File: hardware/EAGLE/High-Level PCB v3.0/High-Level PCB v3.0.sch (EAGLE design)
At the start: 28 parts, among them IC1 DS8921, IC2 DS8921, J1 Micro-SD, J2 Gyro, J3 Compass, J4 GPS, J5 CAN BUS, X1 RJ45, X2 Vehicle control, X4 RJ45

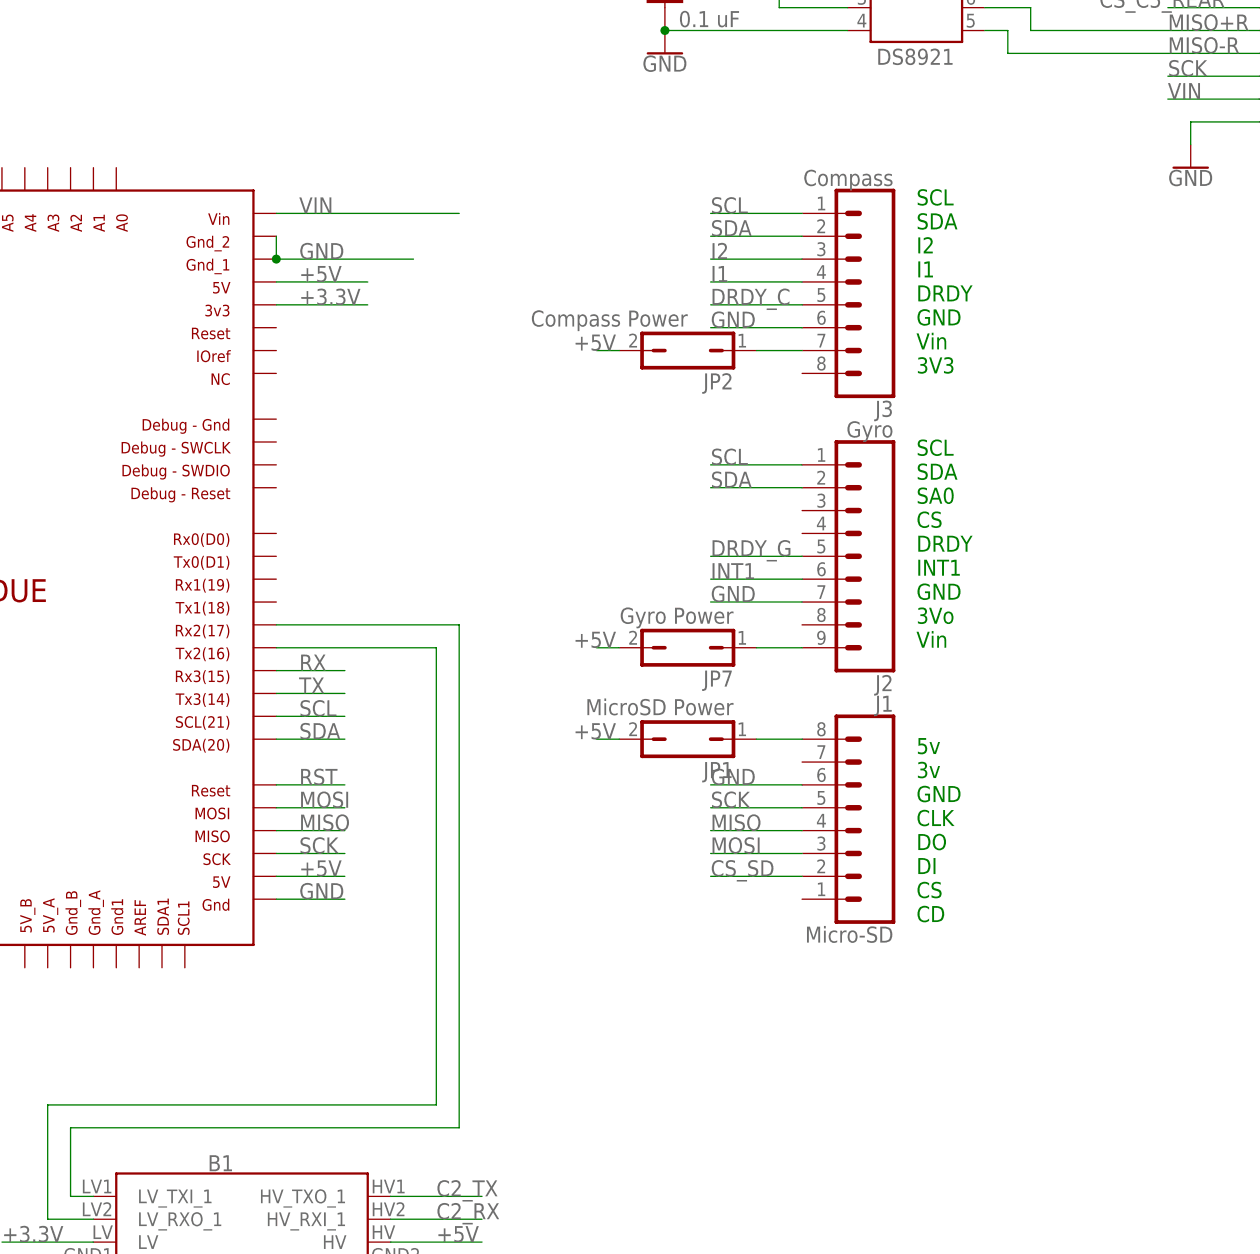
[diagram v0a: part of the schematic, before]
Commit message: Added additional header for compass and moved the i2C to other bus
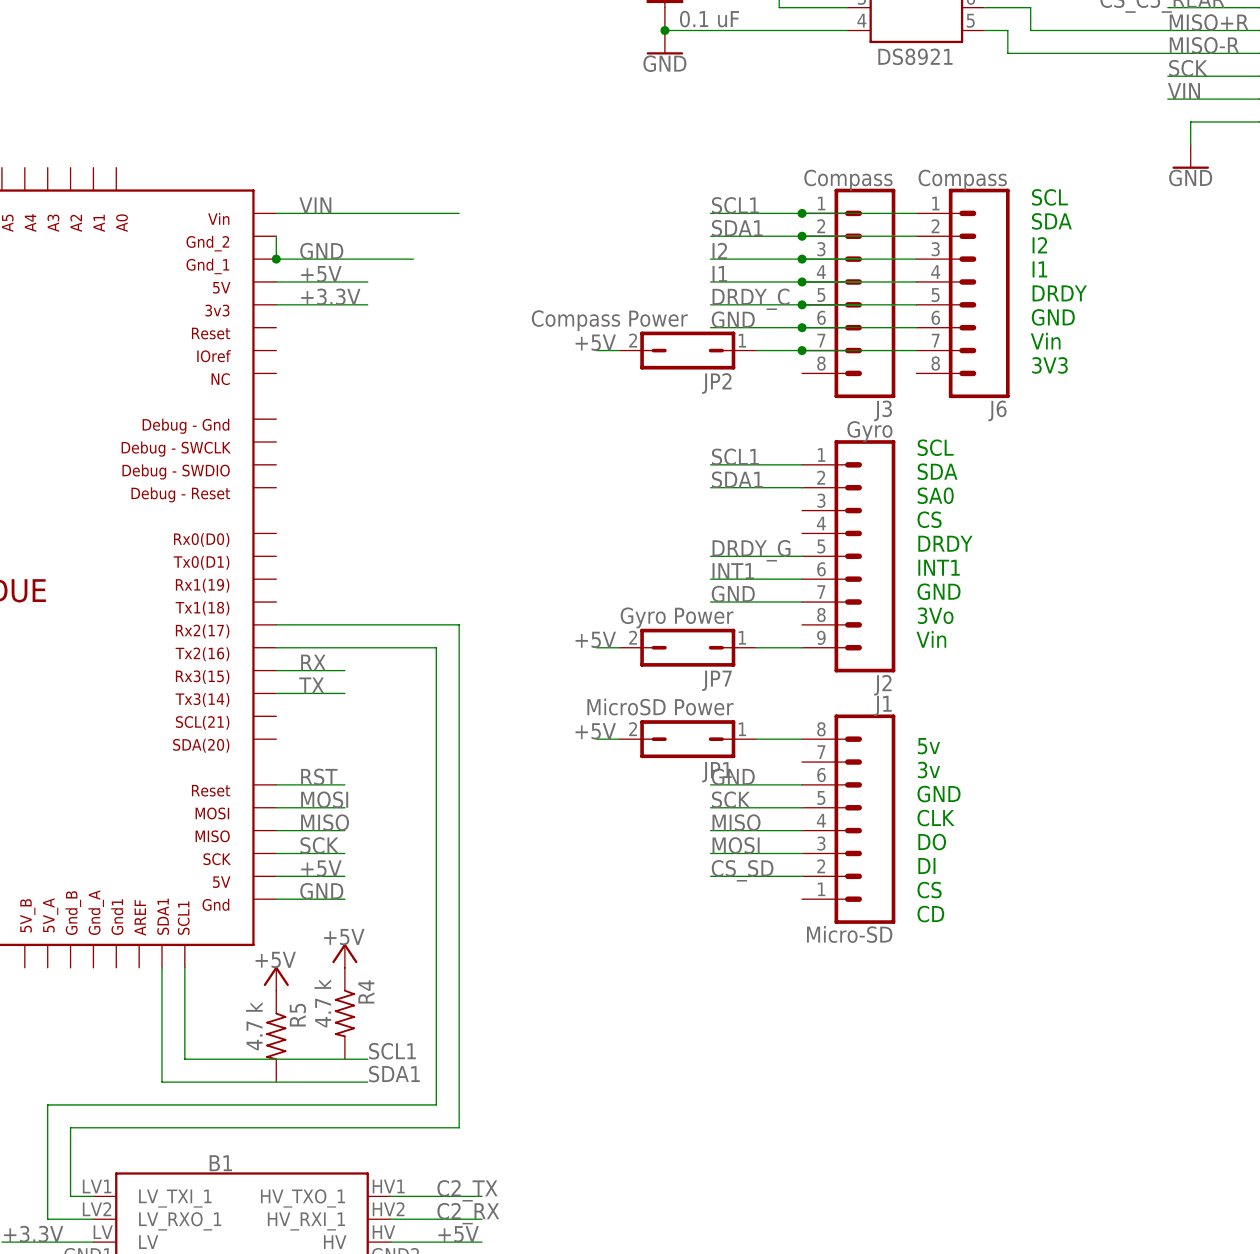
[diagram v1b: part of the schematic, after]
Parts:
- added J6: Compass, SparkFun-Connectors:CONN_08"
- added R4, R5: 4.7 k, resistor:R-US_0204/5
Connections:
- removed net SCL: J2.1, J3.1, U$1.SCL
- removed net SDA: J2.2, J3.2, U$1.SDA
- new net SCL1: J2.1, J3.1, J6.1, U$1.SCL1
- new net SDA1: J2.2, J3.2, J6.2, U$1.SDA1
- net +5V: now also R4.1, R5.1
- net DRDY_C: now also J6.5
- net GND: now also J6.6
- net I1: now also J6.4
- net I2: now also J6.3
- net N$8: now also J6.7
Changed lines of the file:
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@@
 <part name="JP5" library="jumper" library_urn="urn:adsk.eagle:library:252" deviceset="JP1Q" device="" package3d_urn="urn:adsk.eagle:package:15455/1" value="GPS Power"/>
 <part name="FRAME1" library="frames" library_urn="urn:adsk.eagle:library:229" deviceset="FRAME_A_L" device=""/>
+<part name="J6" library="SparkFun-Connectors" deviceset="CONN_08" device="&quot;" value="Compass"/>
+<part name="R4" library="resistor" library_urn="urn:adsk.eagle:library:348" deviceset="R-US_" device="0204/5" package3d_urn="urn:adsk.eagle:package:25955/1" value="4.7 k"/>
+<part name="R5" library="resistor" library_urn="urn:adsk.eagle:library:348" deviceset="R-US_" device="0204/5" package3d_urn="urn:adsk.eagle:package:25955/1" value="4.7 k"/>
+<part name="P+4" library="supply1" library_urn="urn:adsk.eagle:library:371" deviceset="+5V" device=""/>
+<part name="P+6" library="supply1" library_urn="urn:adsk.eagle:library:371" deviceset="+5V" device=""/>
 </parts>
 <sheets>
 <sheet>
 <plain>
-<text x="213.36" y="119.38" size="1.778" layer="91">SCL
+<text x="226.06" y="119.38" size="1.778" layer="91">SCL
 SDA
 I2
@@
 <attribute name="DRAWING_NAME" x="190.5" y="19.05" size="2.54" layer="94"/>
 </instance>
+<instance part="J6" gate="G$1" x="218.44" y="129.54" rot="R180"/>
+<instance part="R4" gate="G$1" x="149.86" y="48.26" rot="R270"/>
+<instance part="R5" gate="G$1" x="142.24" y="45.72" rot="R270"/>
+<instance part="P+4" gate="1" x="149.86" y="55.88" smashed="yes">
+<attribute name="VALUE" x="147.32" y="55.88" size="1.778" layer="96"/>
+</instance>
+<instance part="P+6" gate="1" x="142.24" y="53.34" smashed="yes">
+<attribute name="VALUE" x="139.7" y="53.34" size="1.778" layer="96"/>
+</instance>
 </instances>
 <busses>
@@
 <wire x1="200.66" y1="124.46" x2="190.5" y2="124.46" width="0.1524" layer="91"/>
 <label x="190.5" y="124.46" size="1.778" layer="95"/>
+<pinref part="J6" gate="G$1" pin="6"/>
+<wire x1="200.66" y1="124.46" x2="213.36" y2="124.46" width="0.1524" layer="91"/>
+<junction x="200.66" y="124.46"/>
 </segment>
 <segment>
@@
 </segment>
 </net>
-<net name="SCL" class="0">
-<segment>
-<pinref part="J2" gate="G$1" pin="1"/>
-<wire x1="200.66" y1="109.22" x2="190.5" y2="109.22" width="0.1524" layer="91"/>
-<label x="190.5" y="109.22" size="1.778" layer="95"/>
-</segment>
-<segment>
-<pinref part="U$1" gate="G$1" pin="SCL"/>
-<wire x1="142.24" y1="81.28" x2="149.86" y2="81.28" width="0.1524" layer="91"/>
-<label x="144.78" y="81.28" size="1.778" layer="95"/>
-</segment>
-<segment>
-<pinref part="J3" gate="G$1" pin="1"/>
-<wire x1="200.66" y1="137.16" x2="190.5" y2="137.16" width="0.1524" layer="91"/>
-<label x="190.5" y="137.16" size="1.778" layer="95"/>
-</segment>
-</net>
-<net name="SDA" class="0">
-<segment>
-<pinref part="J2" gate="G$1" pin="2"/>
-<wire x1="200.66" y1="106.68" x2="190.5" y2="106.68" width="0.1524" layer="91"/>
-<label x="190.5" y="106.68" size="1.778" layer="95"/>
-</segment>
-<segment>
-<pinref part="U$1" gate="G$1" pin="SDA"/>
-<wire x1="142.24" y1="78.74" x2="149.86" y2="78.74" width="0.1524" layer="91"/>
-<label x="144.78" y="78.74" size="1.778" layer="95"/>
-</segment>
-<segment>
-<pinref part="J3" gate="G$1" pin="2"/>
-<wire x1="200.66" y1="134.62" x2="190.5" y2="134.62" width="0.1524" layer="91"/>
-<label x="190.5" y="134.62" size="1.778" layer="95"/>
-</segment>
-</net>
 <net name="INT1" class="0">
 <segment>
@@
 <wire x1="200.66" y1="132.08" x2="190.5" y2="132.08" width="0.1524" layer="91"/>
 <label x="190.5" y="132.08" size="1.778" layer="95"/>
+<pinref part="J6" gate="G$1" pin="3"/>
+<wire x1="200.66" y1="132.08" x2="213.36" y2="132.08" width="0.1524" layer="91"/>
+<junction x="200.66" y="132.08"/>
 </segment>
 <segment>
@@
 <wire x1="200.66" y1="129.54" x2="190.5" y2="129.54" width="0.1524" layer="91"/>
 <label x="190.5" y="129.54" size="1.778" layer="95"/>
+<pinref part="J6" gate="G$1" pin="4"/>
+<wire x1="200.66" y1="129.54" x2="213.36" y2="129.54" width="0.1524" layer="91"/>
+<junction x="200.66" y="129.54"/>
 </segment>
 <segment>
@@
 <wire x1="200.66" y1="127" x2="190.5" y2="127" width="0.1524" layer="91"/>
 <label x="190.5" y="127" size="1.778" layer="95"/>
+<pinref part="J6" gate="G$1" pin="5"/>
+<wire x1="200.66" y1="127" x2="213.36" y2="127" width="0.1524" layer="91"/>
+<junction x="200.66" y="127"/>
 </segment>
 <segment>
@@
 <label x="58.42" y="116.84" size="1.778" layer="95" rot="R180"/>
 </segment>
+<segment>
+<pinref part="R4" gate="G$1" pin="1"/>
+<pinref part="P+4" gate="1" pin="+5V"/>
+</segment>
+<segment>
+<pinref part="R5" gate="G$1" pin="1"/>
+<pinref part="P+6" gate="1" pin="+5V"/>
+</segment>
 </net>
 <net name="CANRX" class="0">
@@
 <pinref part="J3" gate="G$1" pin="7"/>
 <wire x1="195.58" y1="121.92" x2="200.66" y2="121.92" width="0.1524" layer="91"/>
+<pinref part="J6" gate="G$1" pin="7"/>
+<wire x1="200.66" y1="121.92" x2="213.36" y2="121.92" width="0.1524" layer="91"/>
+<junction x="200.66" y="121.92"/>
 </segment>
 </net>
@@
 </segment>
 </net>
+<net name="SCL1" class="0">
+<segment>
+<pinref part="U$1" gate="G$1" pin="SCL1"/>
+<wire x1="132.08" y1="53.34" x2="132.08" y2="43.18" width="0.1524" layer="91"/>
+<wire x1="132.08" y1="43.18" x2="152.4" y2="43.18" width="0.1524" layer="91"/>
+<label x="152.4" y="43.18" size="1.778" layer="95"/>
+</segment>
+<segment>
+<pinref part="J2" gate="G$1" pin="1"/>
+<wire x1="200.66" y1="109.22" x2="190.5" y2="109.22" width="0.1524" layer="91"/>
+<label x="190.5" y="109.22" size="1.778" layer="95"/>
+</segment>
+<segment>
+<pinref part="J3" gate="G$1" pin="1"/>
+<wire x1="200.66" y1="137.16" x2="190.5" y2="137.16" width="0.1524" layer="91"/>
+<label x="190.5" y="137.16" size="1.778" layer="95"/>
+<pinref part="J6" gate="G$1" pin="1"/>
+<wire x1="200.66" y1="137.16" x2="213.36" y2="137.16" width="0.1524" layer="91"/>
+<junction x="200.66" y="137.16"/>
+</segment>
+</net>
+<net name="SDA1" class="0">
+<segment>
+<pinref part="U$1" gate="G$1" pin="SDA1"/>
+<wire x1="129.54" y1="53.34" x2="129.54" y2="40.64" width="0.1524" layer="91"/>
+<wire x1="129.54" y1="40.64" x2="152.4" y2="40.64" width="0.1524" layer="91"/>
+<label x="152.4" y="40.64" size="1.778" layer="95"/>
+</segment>
+<segment>
+<pinref part="J2" gate="G$1" pin="2"/>
+<wire x1="200.66" y1="106.68" x2="190.5" y2="106.68" width="0.1524" layer="91"/>
+<label x="190.5" y="106.68" size="1.778" layer="95"/>
+</segment>
+<segment>
+<pinref part="J3" gate="G$1" pin="2"/>
+<wire x1="200.66" y1="134.62" x2="190.5" y2="134.62" width="0.1524" layer="91"/>
+<label x="190.5" y="134.62" size="1.778" layer="95"/>
+<pinref part="J6" gate="G$1" pin="2"/>
+<wire x1="200.66" y1="134.62" x2="213.36" y2="134.62" width="0.1524" layer="91"/>
+<junction x="200.66" y="134.62"/>
+</segment>
+</net>

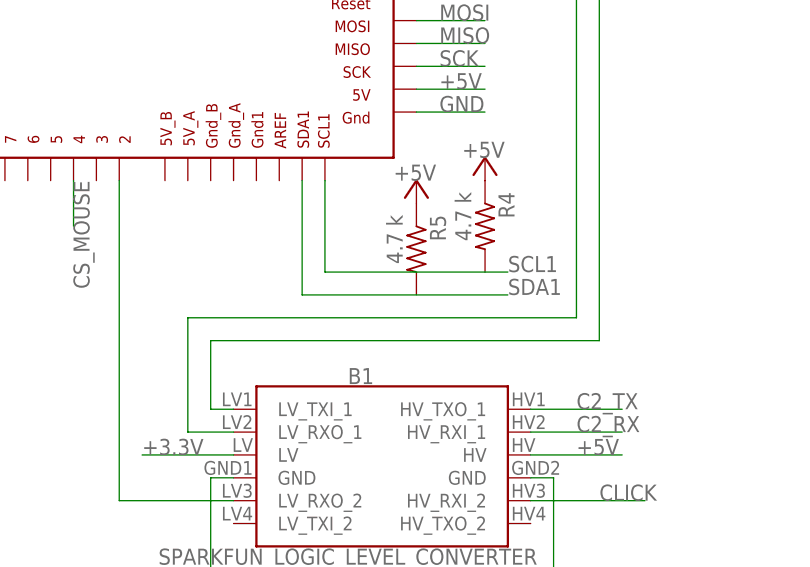
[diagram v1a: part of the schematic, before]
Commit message: Fixed pull-up resistors on I2C bus
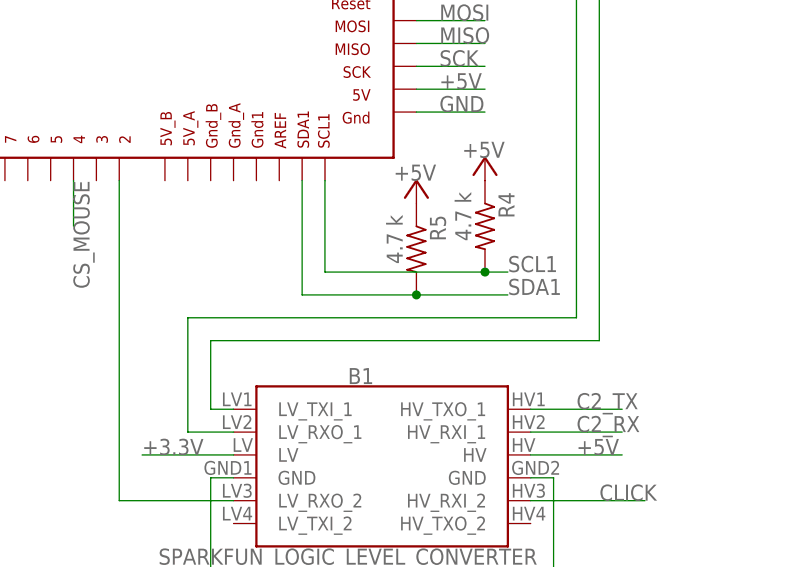
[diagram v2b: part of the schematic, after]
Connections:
- net SCL1: now also R4.2
- net SDA1: now also R5.2
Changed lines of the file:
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@@
 <pinref part="U$1" gate="G$1" pin="SCL1"/>
 <wire x1="132.08" y1="53.34" x2="132.08" y2="43.18" width="0.1524" layer="91"/>
-<wire x1="132.08" y1="43.18" x2="152.4" y2="43.18" width="0.1524" layer="91"/>
+<wire x1="132.08" y1="43.18" x2="149.86" y2="43.18" width="0.1524" layer="91"/>
 <label x="152.4" y="43.18" size="1.778" layer="95"/>
+<pinref part="R4" gate="G$1" pin="2"/>
+<wire x1="149.86" y1="43.18" x2="152.4" y2="43.18" width="0.1524" layer="91"/>
+<junction x="149.86" y="43.18"/>
 </segment>
 <segment>
@@
 <pinref part="U$1" gate="G$1" pin="SDA1"/>
 <wire x1="129.54" y1="53.34" x2="129.54" y2="40.64" width="0.1524" layer="91"/>
-<wire x1="129.54" y1="40.64" x2="152.4" y2="40.64" width="0.1524" layer="91"/>
+<wire x1="129.54" y1="40.64" x2="142.24" y2="40.64" width="0.1524" layer="91"/>
 <label x="152.4" y="40.64" size="1.778" layer="95"/>
+<pinref part="R5" gate="G$1" pin="2"/>
+<wire x1="142.24" y1="40.64" x2="152.4" y2="40.64" width="0.1524" layer="91"/>
+<junction x="142.24" y="40.64"/>
 </segment>
 <segment>
